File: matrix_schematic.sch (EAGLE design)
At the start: 4 parts, among them IC1 74LS595D, IC2 74LS595D, IC3 74LS595D

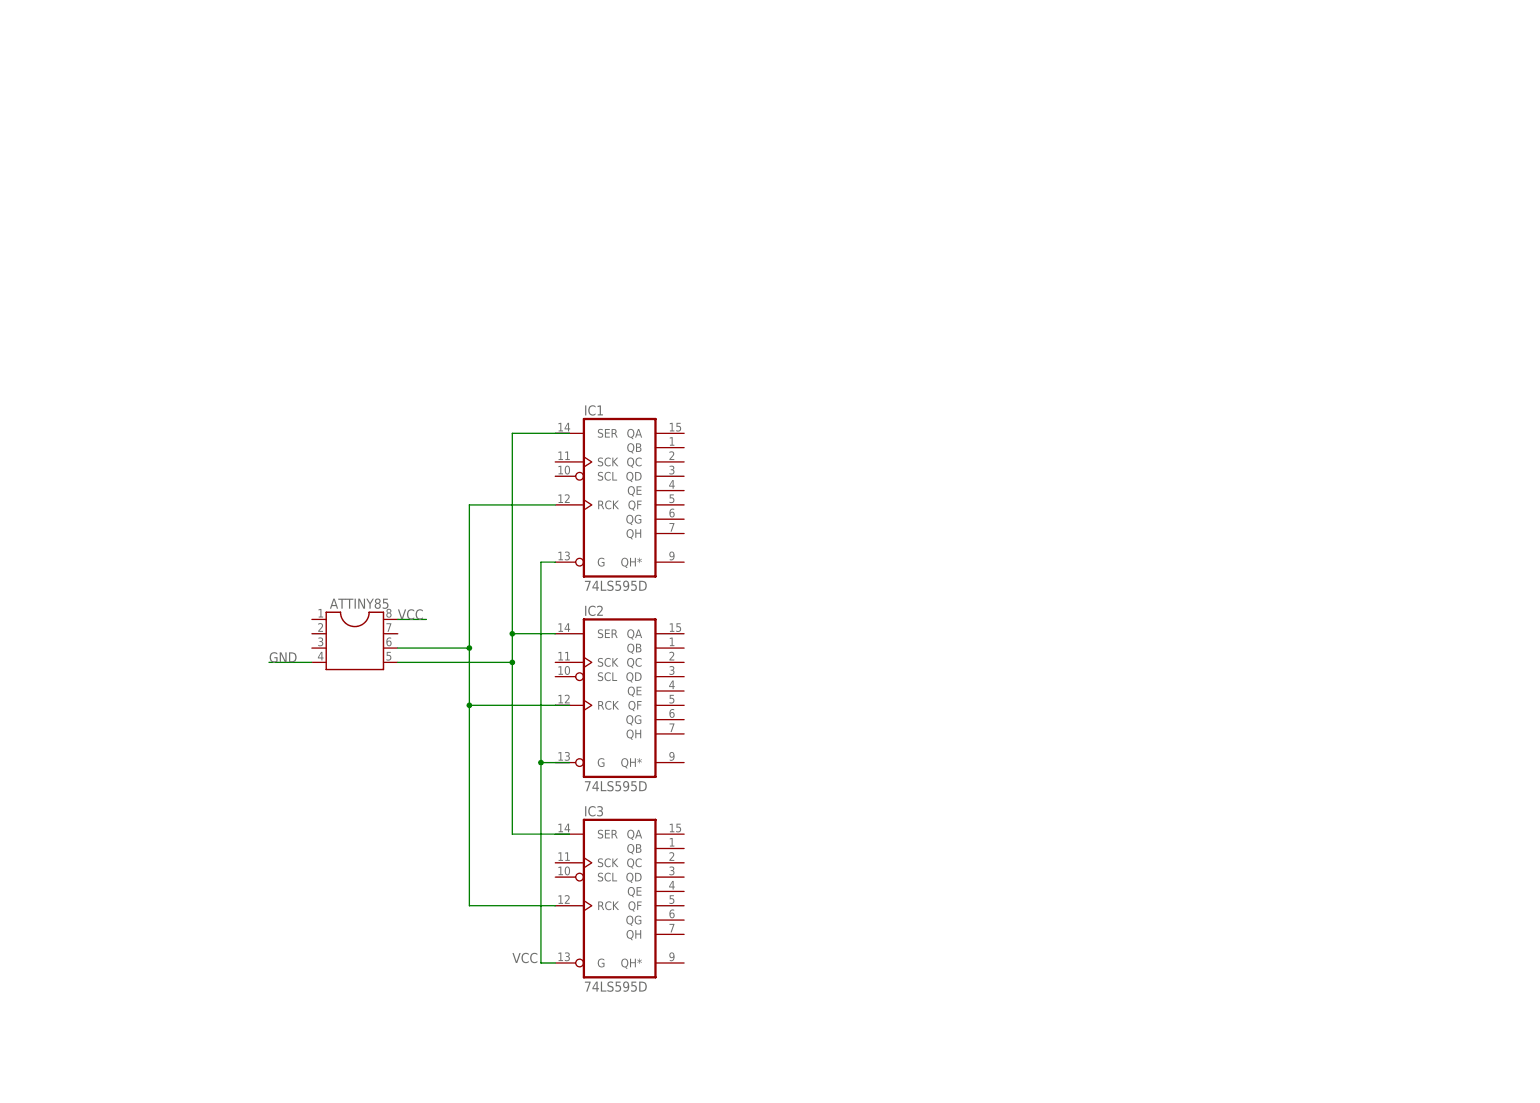
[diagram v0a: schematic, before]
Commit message: Finished initial schematic
Uses ATTINY85 with three 74-595s each with their own serial in from the
ATTINY85. One used for ground connections on the matrix, two used for
anode connections for controlling color. BS270 N-Channel Mosfets used
for draining current on each row.
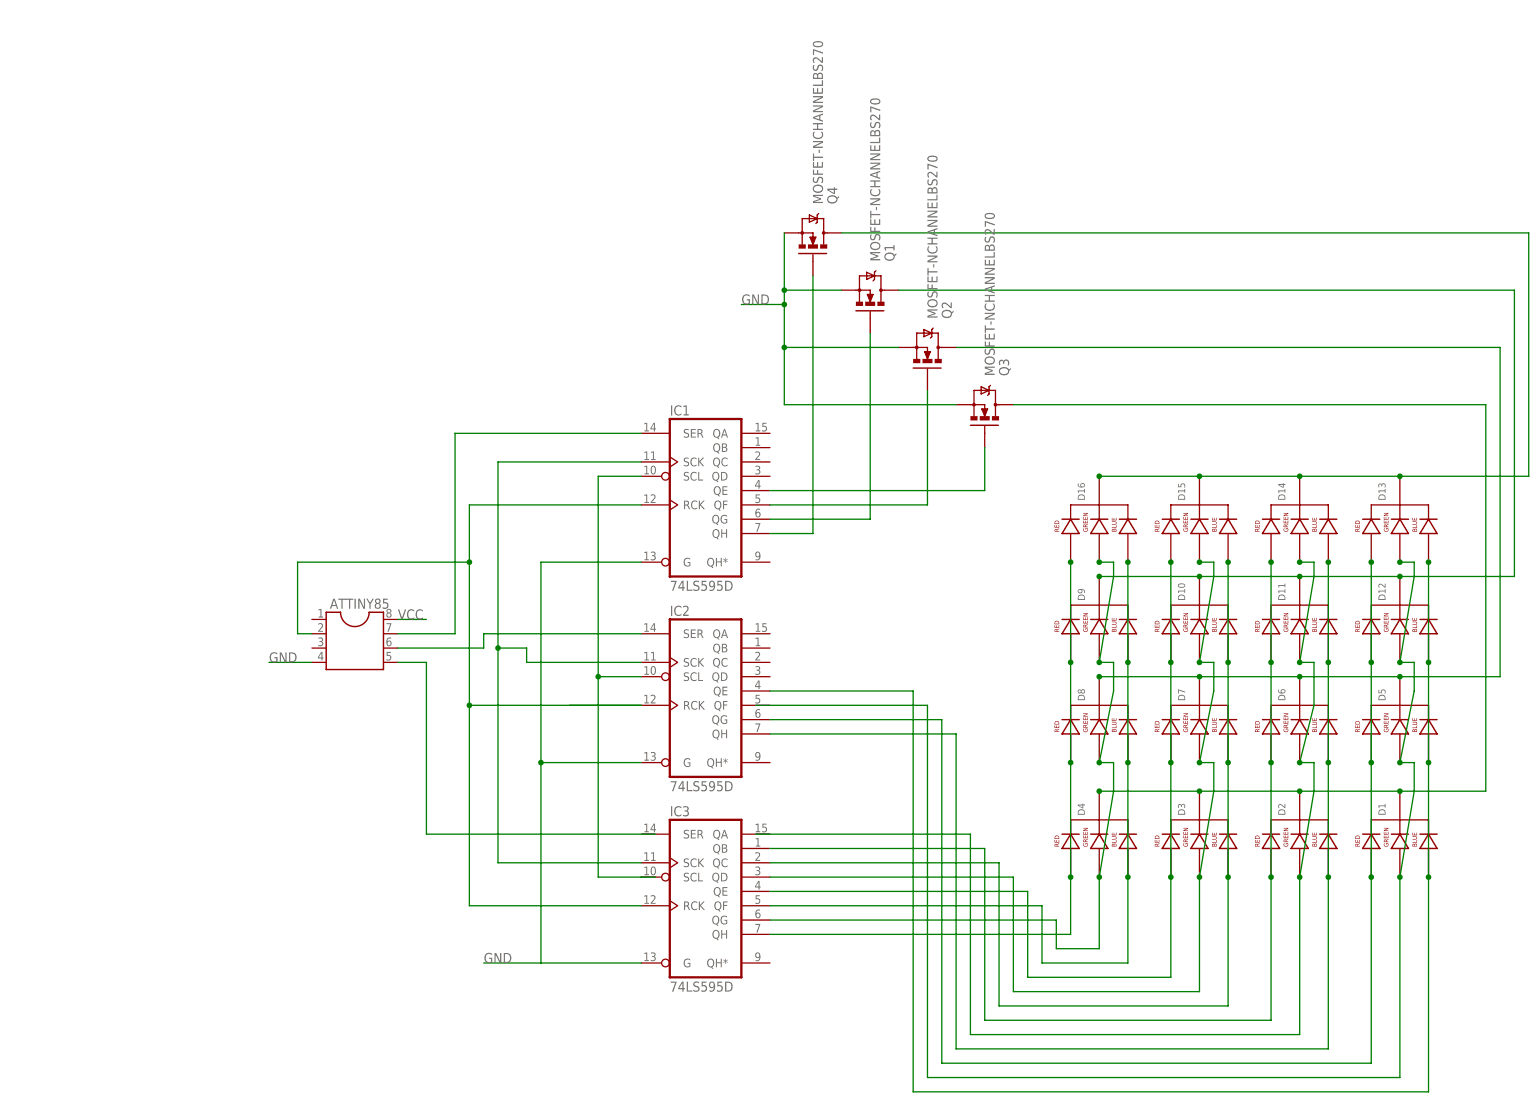
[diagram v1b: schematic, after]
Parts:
- added D1, D10, D11, D12, D13, D14, D15, D16, D2, D3, D4, D5, D6, D7, D8, D9: LED-RGB-CC-THRUDIFFUSE, SparkFun-LED:LED-RGB-CC-THRUDIFFUSE
- added Q1, Q2, Q3, Q4: MOSFET-NCHANNELBS270, SparkFun-DiscreteSemi:MOSFET-NCHANNELBS170
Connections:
- removed net N$1: ATTINY85.5, IC1A.SER, IC2A.SER
- new net N$10: D11.RED_CATHODE, D14.RED_CATHODE, D2.RED_CATHODE, D6.RED_CATHODE, IC3A.QB
- new net N$11: D10.BLUE_CATHODE, D15.BLUE_CATHODE, D3.BLUE_CATHODE, D7.BLUE_CATHODE, IC3A.QC
- new net N$12: D10.GREEN_CATHODE, D15.GREEN_CATHODE, D3.GREEN_CATHODE, D7.GREEN_CATHODE, IC3A.QD
- new net N$13: D10.RED_CATHODE, D15.RED_CATHODE, D3.RED_CATHODE, D7.RED_CATHODE, IC3A.QE
- new net N$14: D16.BLUE_CATHODE, D4.BLUE_CATHODE, D8.BLUE_CATHODE, D9.BLUE_CATHODE, IC3A.QF
- new net N$15: D16.GREEN_CATHODE, D4.GREEN_CATHODE, D8.GREEN_CATHODE, D9.GREEN_CATHODE, IC3A.QG
- new net N$16: D16.RED_CATHODE, D4.RED_CATHODE, D8.RED_CATHODE, D9.RED_CATHODE, IC3A.QH
- new net N$17: D13.CATHODE, D14.CATHODE, D15.CATHODE, D16.CATHODE, Q4.D
- new net N$18: D1.CATHODE, D2.CATHODE, D3.CATHODE, D4.CATHODE, Q3.D
- new net N$19: D5.CATHODE, D6.CATHODE, D7.CATHODE, D8.CATHODE, Q2.D
- new net N$20: D10.CATHODE, D11.CATHODE, D12.CATHODE, D9.CATHODE, Q1.D
- new net N$21: ATTINY85.7, IC1A.SER
- new net N$22: ATTINY85.6, IC2A.SER
- new net N$23: ATTINY85.5
- new net N$27: IC1A.QH, Q4.G
- new net N$28: IC1A.QG, Q1.G
- new net N$29: IC1A.QF, Q2.G
- new net N$3: IC1A.SCK, IC2A.SCK, IC3A.SCK
- new net N$30: IC1A.QE, Q3.G
- new net N$4: D1.GREEN_CATHODE, D12.GREEN_CATHODE, D13.GREEN_CATHODE, D5.GREEN_CATHODE
- new net N$5: IC1A.SCL, IC2A.SCL, IC3A.SCL
- new net N$6: D1.BLUE_CATHODE, D12.BLUE_CATHODE, D13.BLUE_CATHODE, D5.BLUE_CATHODE, IC2A.QE
- new net N$7: D1.RED_CATHODE, D12.RED_CATHODE, D13.RED_CATHODE, D5.RED_CATHODE, IC2A.QG
- new net N$8: D11.BLUE_CATHODE, D14.BLUE_CATHODE, D2.BLUE_CATHODE, D6.BLUE_CATHODE, IC2A.QH
- new net N$9: D11.GREEN_CATHODE, D14.GREEN_CATHODE, D2.GREEN_CATHODE, D6.GREEN_CATHODE
- net GND: now also IC1A.G, IC2A.G, IC3A.G, Q1.S, Q2.S, Q3.S, Q4.S
- net N$2: now also ATTINY85.2; no longer ATTINY85.6
- net VCC: no longer IC1A.G, IC3A.G
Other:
- moved on the sheet: IC1, IC2, IC3

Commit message: Initial commit of board layout and fixes to schematic
One airwire left on board and optimization needed as there are a bunch
of uneccesary traces.
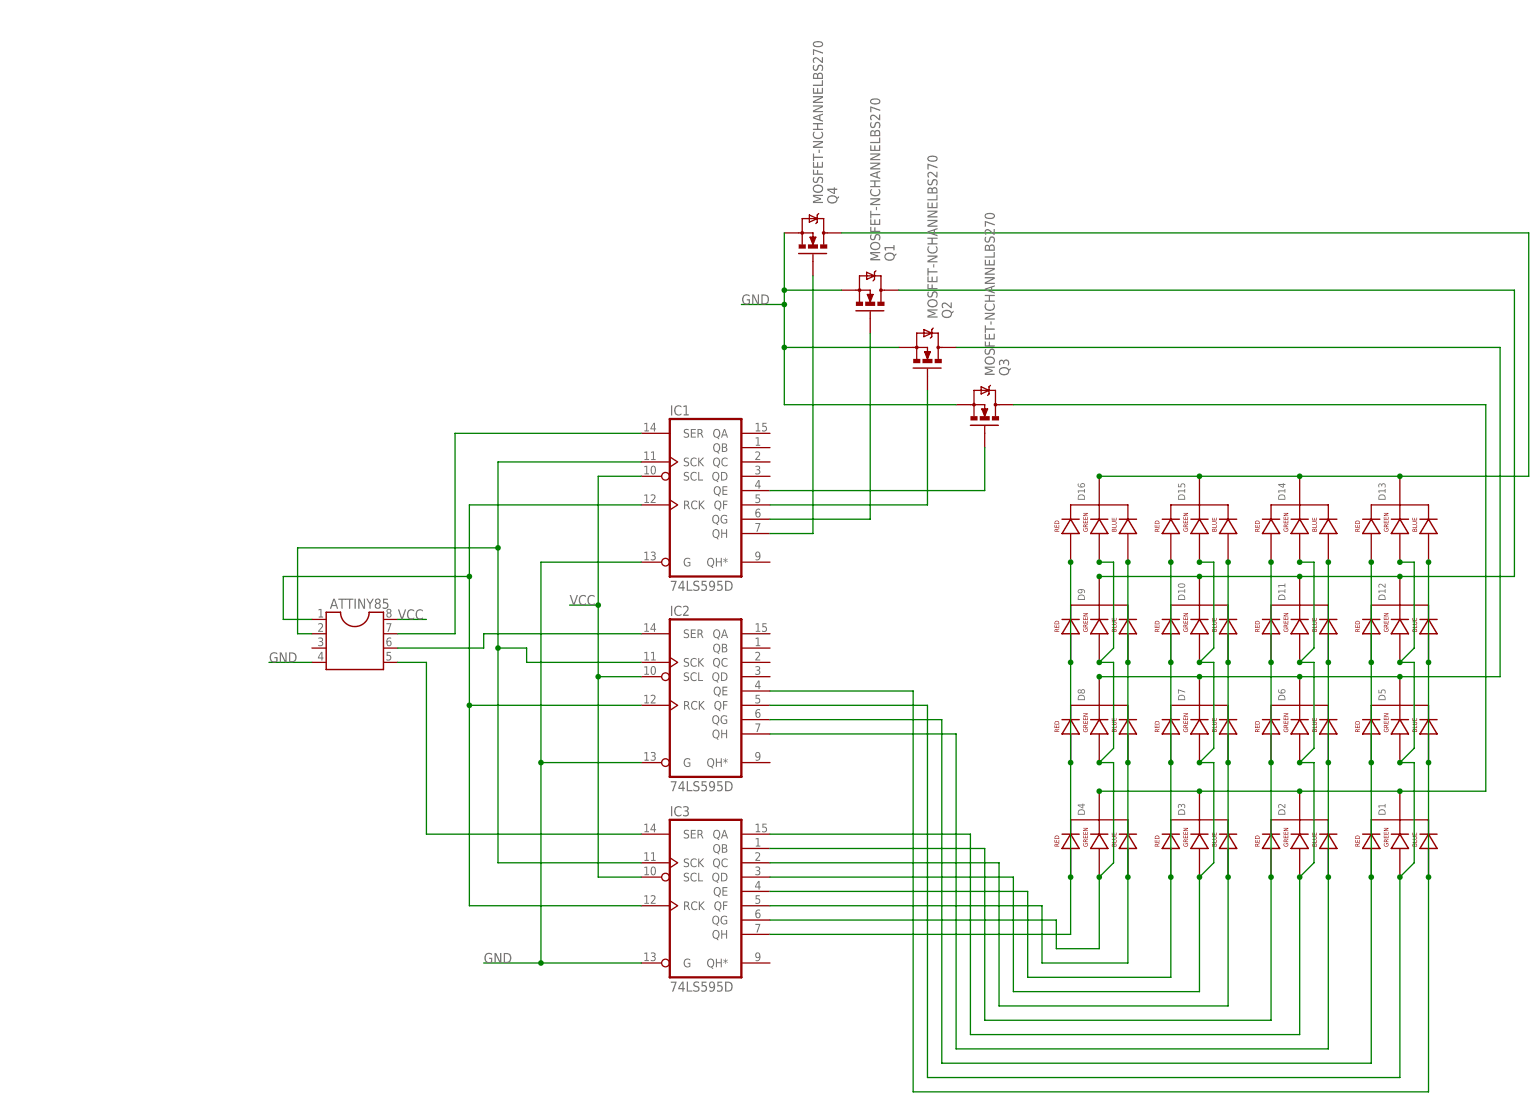
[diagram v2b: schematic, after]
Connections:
- removed net N$5: IC1A.SCL, IC2A.SCL, IC3A.SCL
- net N$2: now also ATTINY85.1; no longer ATTINY85.2
- net N$23: now also IC3A.SER
- net N$3: now also ATTINY85.2
- net N$4: now also IC2A.QF
- net N$9: now also IC3A.QA
- net VCC: now also IC1A.SCL, IC2A.SCL, IC3A.SCL

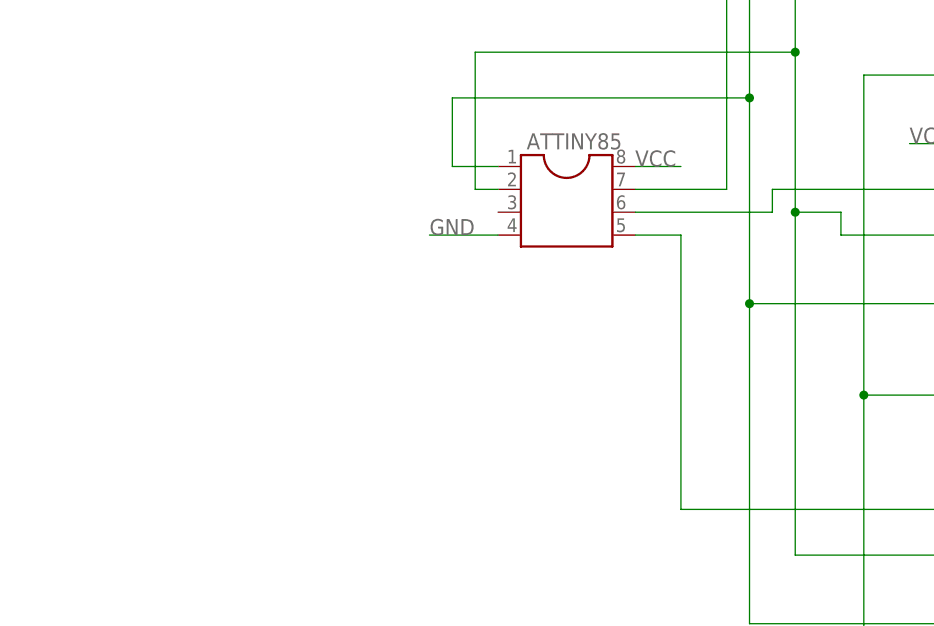
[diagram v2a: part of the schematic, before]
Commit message: Added ISP header for programming
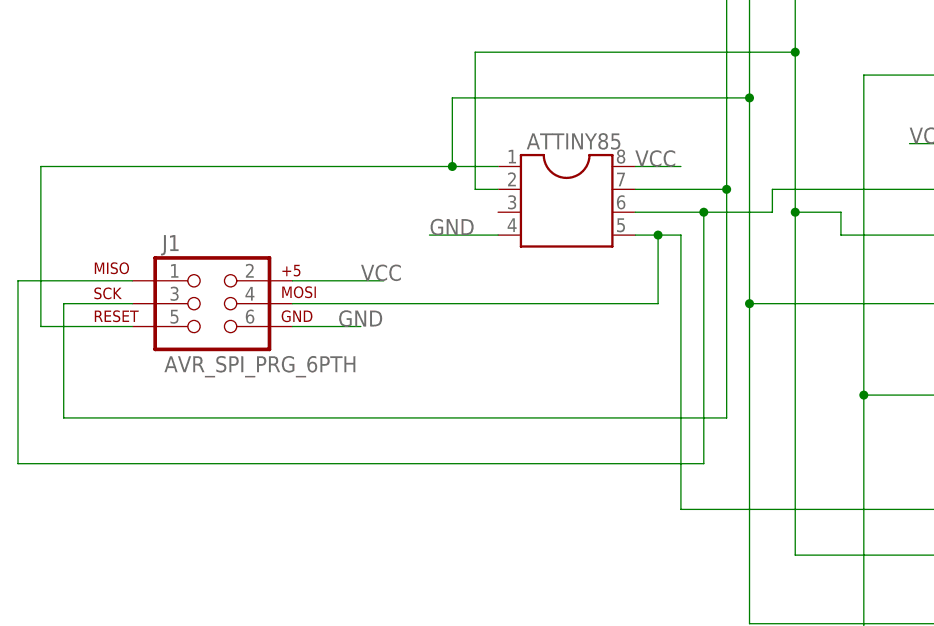
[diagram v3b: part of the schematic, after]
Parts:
- added J1: AVR_SPI_PRG_6PTH, SparkFun-Connectors:AVR_SPI_PRG_6PTH
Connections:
- net GND: now also J1.6
- net N$2: now also J1.5
- net N$21: now also J1.3
- net N$22: now also J1.1
- net N$23: now also J1.4
- net VCC: now also J1.2
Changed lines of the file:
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@@
 <layers>
 <layer number="1" name="Top" color="4" fill="1" visible="no" active="no"/>
+<layer number="2" name="Route2" color="1" fill="3" visible="no" active="no"/>
+<layer number="3" name="Route3" color="4" fill="3" visible="no" active="no"/>
+<layer number="4" name="Route4" color="1" fill="4" visible="no" active="no"/>
+<layer number="5" name="Route5" color="4" fill="4" visible="no" active="no"/>
+<layer number="6" name="Route6" color="1" fill="8" visible="no" active="no"/>
+<layer number="7" name="Route7" color="4" fill="8" visible="no" active="no"/>
+<layer number="8" name="Route8" color="1" fill="2" visible="no" active="no"/>
+<layer number="9" name="Route9" color="4" fill="2" visible="no" active="no"/>
+<layer number="10" name="Route10" color="1" fill="7" visible="no" active="no"/>
+<layer number="11" name="Route11" color="4" fill="7" visible="no" active="no"/>
+<layer number="12" name="Route12" color="1" fill="5" visible="no" active="no"/>
+<layer number="13" name="Route13" color="4" fill="5" visible="no" active="no"/>
+<layer number="14" name="Route14" color="1" fill="6" visible="no" active="no"/>
+<layer number="15" name="Route15" color="4" fill="6" visible="no" active="no"/>
 <layer number="16" name="Bottom" color="1" fill="1" visible="no" active="no"/>
 <layer number="17" name="Pads" color="2" fill="1" visible="no" active="no"/>
@@
 <layer number="144" name="Drill_legend" color="7" fill="1" visible="no" active="yes"/>
 <layer number="151" name="HeatSink" color="7" fill="1" visible="no" active="yes"/>
+<layer number="199" name="Contour" color="7" fill="1" visible="yes" active="yes"/>
 <layer number="200" name="200bmp" color="1" fill="10" visible="no" active="yes"/>
 <layer number="201" name="201bmp" color="2" fill="10" visible="no" active="yes"/>
@@
 <part name="Q3" library="SparkFun-DiscreteSemi" deviceset="MOSFET-NCHANNEL" device="BS170" value="MOSFET-NCHANNELBS270"/>
 <part name="Q4" library="SparkFun-DiscreteSemi" deviceset="MOSFET-NCHANNEL" device="BS170" value="MOSFET-NCHANNELBS270"/>
+<part name="J1" library="SparkFun-Connectors" deviceset="AVR_SPI_PRG_6" device="PTH"/>
 </parts>
 <sheets>
@@
 <instance part="Q3" gate="G$1" x="111.76" y="40.64" rot="MR90"/>
 <instance part="Q4" gate="G$1" x="81.28" y="71.12" rot="MR90"/>
+<instance part="J1" gate="G$1" x="-40.64" y="-12.7"/>
 </instances>
 <busses>
@@
 <label x="38.1" y="5.08" size="1.778" layer="95"/>
 <junction x="43.18" y="5.08"/>
+</segment>
+<segment>
+<pinref part="J1" gate="G$1" pin="2"/>
+<wire x1="-30.48" y1="-10.16" x2="-20.32" y2="-10.16" width="0.1524" layer="91"/>
+<label x="-22.86" y="-10.16" size="1.778" layer="95"/>
 </segment>
 </net>
@@
 <label x="68.58" y="58.42" size="1.778" layer="95"/>
 </segment>
+<segment>
+<pinref part="J1" gate="G$1" pin="6"/>
+<wire x1="-30.48" y1="-15.24" x2="-22.86" y2="-15.24" width="0.1524" layer="91"/>
+<label x="-25.4" y="-15.24" size="1.778" layer="95"/>
+</segment>
 </net>
 <net name="N$2" class="0">
@@
 <pinref part="IC3" gate="A" pin="RCK"/>
 <wire x1="20.32" y1="-48.26" x2="50.8" y2="-48.26" width="0.1524" layer="91"/>
+<pinref part="J1" gate="G$1" pin="5"/>
+<wire x1="-48.26" y1="-15.24" x2="-58.42" y2="-15.24" width="0.1524" layer="91"/>
+<wire x1="-58.42" y1="-15.24" x2="-58.42" y2="2.54" width="0.1524" layer="91"/>
+<wire x1="-58.42" y1="2.54" x2="-12.7" y2="2.54" width="0.1524" layer="91"/>
+<junction x="-12.7" y="2.54"/>
 </segment>
 </net>
@@
 <pinref part="ATTINY85" gate="G$1" pin="7"/>
 <wire x1="17.78" y1="0" x2="7.62" y2="0" width="0.1524" layer="91"/>
+<wire x1="17.78" y1="0" x2="17.78" y2="-25.4" width="0.1524" layer="91"/>
+<wire x1="17.78" y1="-25.4" x2="-55.88" y2="-25.4" width="0.1524" layer="91"/>
+<wire x1="-55.88" y1="-25.4" x2="-55.88" y2="-12.7" width="0.1524" layer="91"/>
+<pinref part="J1" gate="G$1" pin="3"/>
+<wire x1="-55.88" y1="-12.7" x2="-48.26" y2="-12.7" width="0.1524" layer="91"/>
+<junction x="17.78" y="0"/>
 </segment>
 </net>
@@
 <wire x1="22.86" y1="0" x2="22.86" y2="-2.54" width="0.1524" layer="91"/>
 <pinref part="ATTINY85" gate="G$1" pin="6"/>
-<wire x1="22.86" y1="-2.54" x2="7.62" y2="-2.54" width="0.1524" layer="91"/>
+<wire x1="22.86" y1="-2.54" x2="15.24" y2="-2.54" width="0.1524" layer="91"/>
+<pinref part="J1" gate="G$1" pin="1"/>
+<wire x1="15.24" y1="-2.54" x2="7.62" y2="-2.54" width="0.1524" layer="91"/>
+<wire x1="-48.26" y1="-10.16" x2="-60.96" y2="-10.16" width="0.1524" layer="91"/>
+<wire x1="-60.96" y1="-10.16" x2="-60.96" y2="-30.48" width="0.1524" layer="91"/>
+<wire x1="-60.96" y1="-30.48" x2="15.24" y2="-30.48" width="0.1524" layer="91"/>
+<wire x1="15.24" y1="-30.48" x2="15.24" y2="-2.54" width="0.1524" layer="91"/>
+<junction x="15.24" y="-2.54"/>
 </segment>
 </net>
@@
 <wire x1="12.7" y1="-35.56" x2="12.7" y2="-5.08" width="0.1524" layer="91"/>
 <pinref part="ATTINY85" gate="G$1" pin="5"/>
-<wire x1="12.7" y1="-5.08" x2="7.62" y2="-5.08" width="0.1524" layer="91"/>
+<wire x1="12.7" y1="-5.08" x2="10.16" y2="-5.08" width="0.1524" layer="91"/>
 <pinref part="IC3" gate="A" pin="SER"/>
+<pinref part="J1" gate="G$1" pin="4"/>
+<wire x1="10.16" y1="-5.08" x2="7.62" y2="-5.08" width="0.1524" layer="91"/>
+<wire x1="-30.48" y1="-12.7" x2="10.16" y2="-12.7" width="0.1524" layer="91"/>
+<wire x1="10.16" y1="-12.7" x2="10.16" y2="-5.08" width="0.1524" layer="91"/>
+<junction x="10.16" y="-5.08"/>
 </segment>
 </net>
@@
 </sheet>
 </sheets>
+<errors>
+</errors>
 </schematic>
 </drawing>
